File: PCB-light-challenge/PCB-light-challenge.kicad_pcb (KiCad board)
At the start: 4 copper layers, 79.9 x 79 mm, 27 parts, among them J1 Conn_01x16_Socket, J3 Conn_01x13_Socket, U2 AP9101CK, U3 SP8K32FRATB

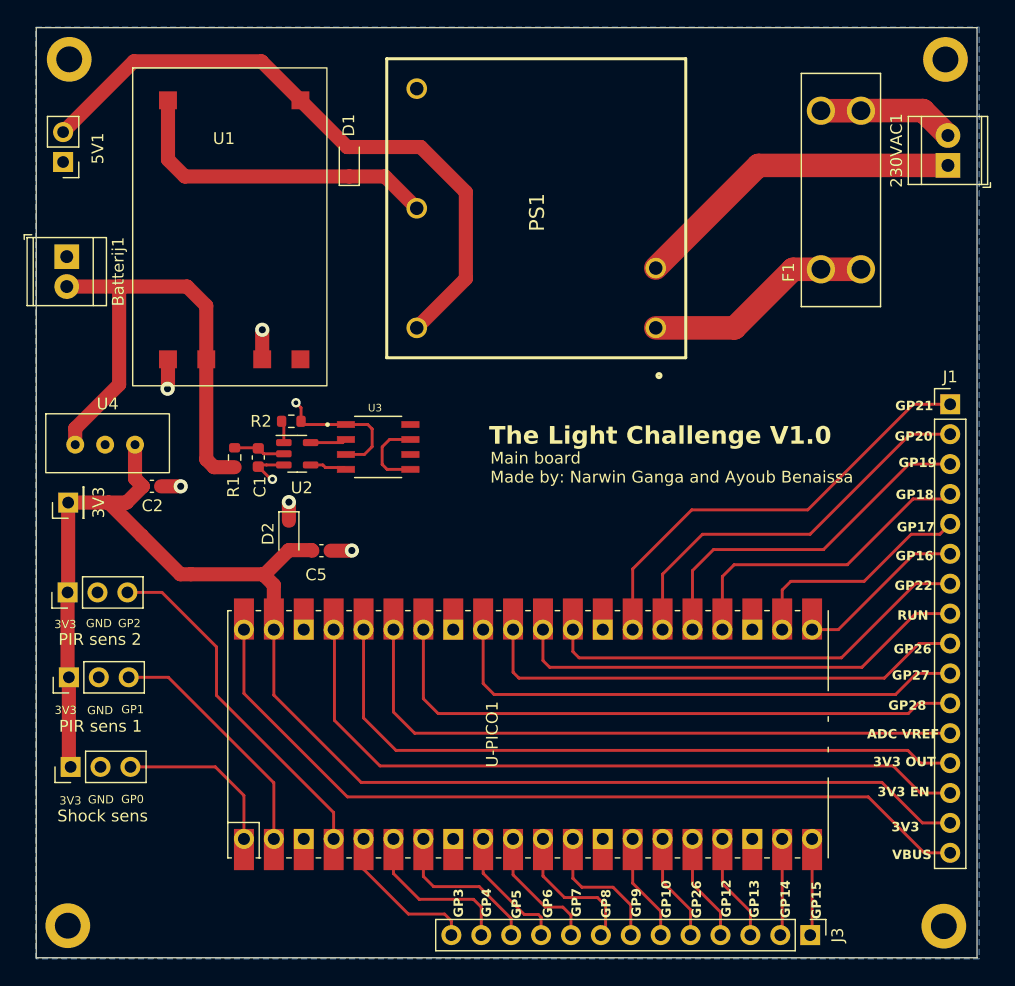
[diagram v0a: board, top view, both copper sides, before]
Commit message: Footprint van de eds protection device aangepast naar sod 523
https://nl.farnell.com/en-NL/rohm/rsb6-8smt2n/esd-protection-diode-sod-523-2/dp/2914120
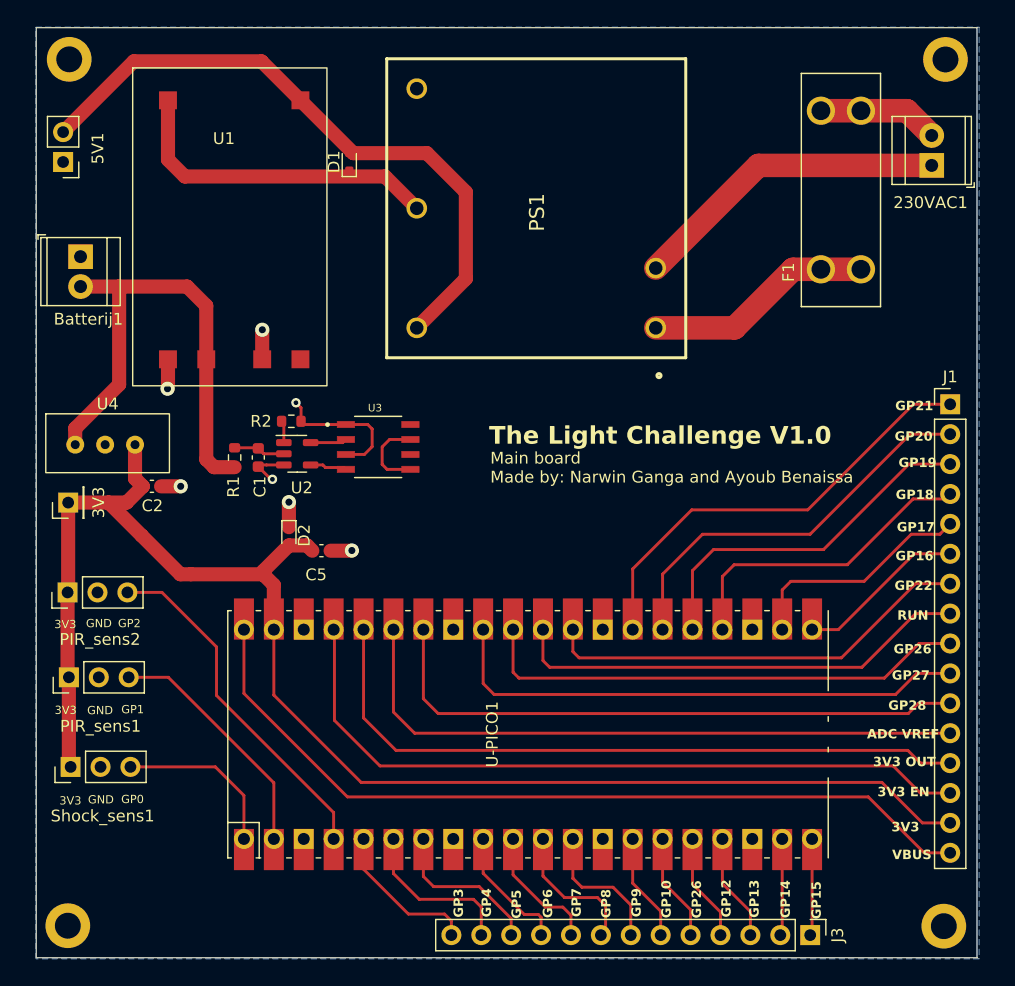
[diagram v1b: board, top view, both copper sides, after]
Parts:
- D1, D2: footprint Diode_SMD:D_SOD-323_HandSoldering -> Diode_SMD:D_SOD-523
- PIR_sens1: renamed from PIR sens 1
- PIR_sens2: renamed from PIR sens 2
- Shock_sens1: renamed from Shock sens
- moved 230VAC1 1.38 mm to (248.5, 84.8)
- moved Batterij1 1.17 mm to (176.2, 92.6)
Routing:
- net /Battery_charger/GNDAC: track 28.4 -> 27.1 mm
- net /Battery_charger/Fuse_in: track 11.7 -> 10.3 mm
- net BAT+: track 43.7 -> 42.5 mm
- net GND: track 26.0 -> 26.6 mm

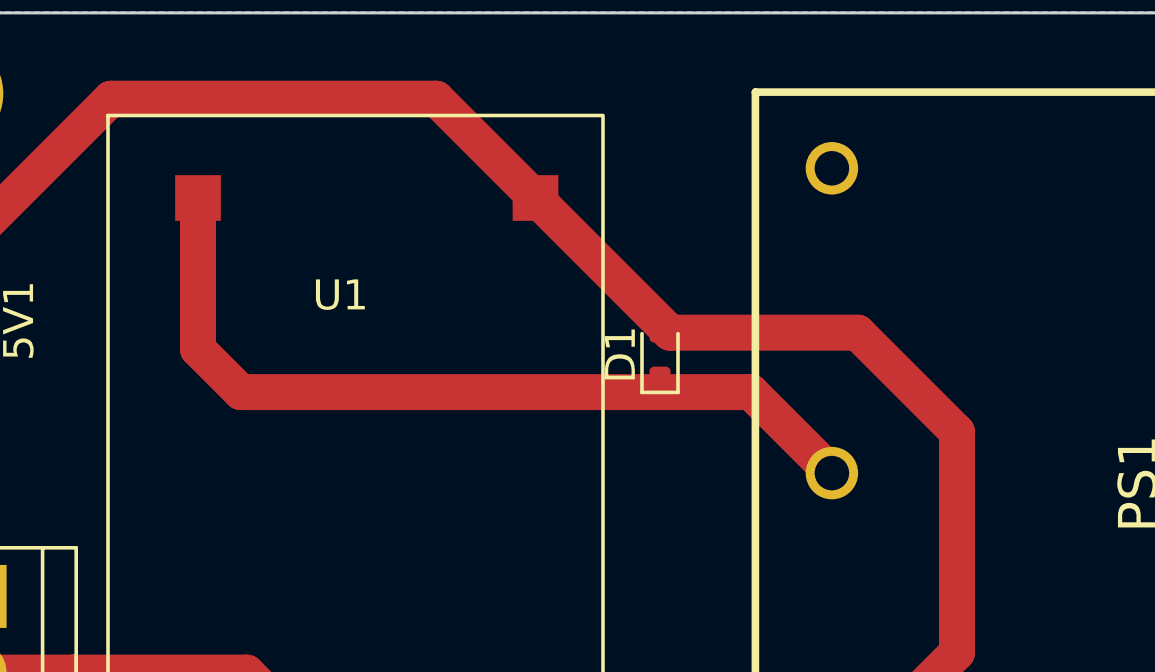
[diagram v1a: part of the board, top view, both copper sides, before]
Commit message: EDS device bij 230 verwijdert
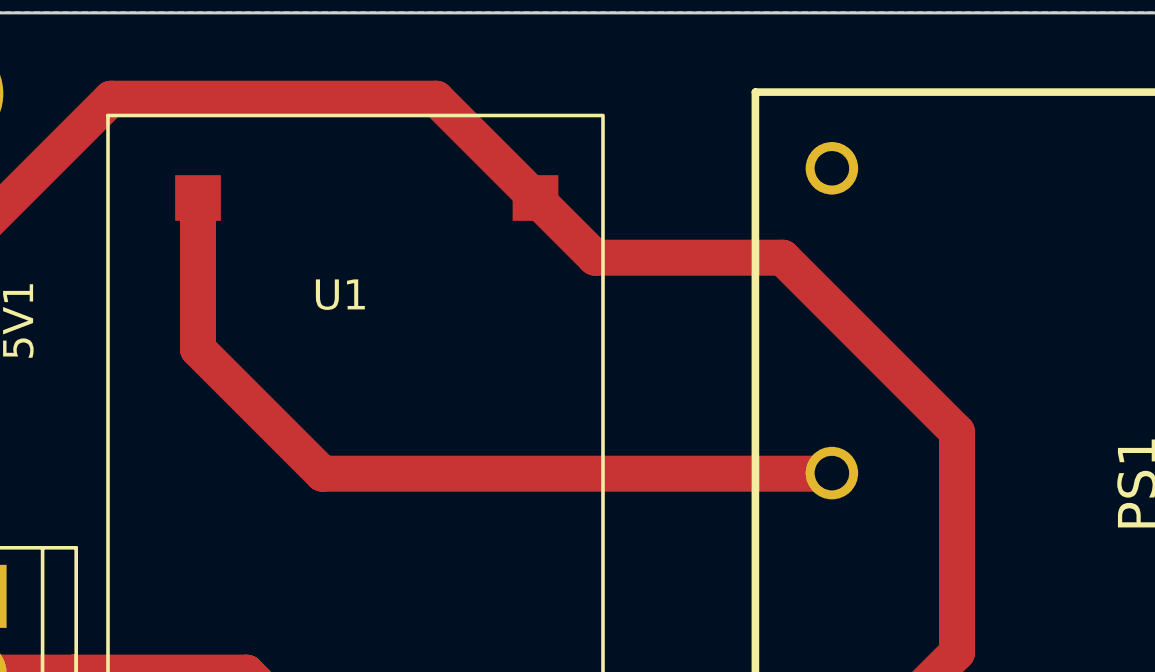
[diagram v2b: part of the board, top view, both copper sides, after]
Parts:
- removed D1: ESD9B3.3ST5G, Diode_SMD:D_SOD-523
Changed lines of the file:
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@@
   (net 40 "Net-(U3-Pad5)")
   (net 41 "GND")
-  (net 42 "Net-(D1-A1)")
+  (net 42 "Net-(PS1--VOUT)")
   (net 43 "/Battery_charger/Fuse_in")
   (net 44 "/Battery_charger/Fuse")
@@
       (scale (xyz 1 1 1))
       (rotate (xyz -90 0 0))
-    )
-  )
-  (footprint "Diode_SMD:D_SOD-523" (layer "F.Cu")
-    (at 199.03 84.53 90)
-    (descr "http://www.diodes.com/datasheets/ap02001.pdf p.144")
-    (tags "Diode SOD523")
-    (property "Sheetfile" "Battery_charger.kicad_sch")
-    (property "Sheetname" "Battery_charger")
-    (property "ki_description" "ESD protection diode, 3.3Vrwm, SOD-923")
-    (property "ki_keywords" "diode TVS ESD")
-    (attr smd)
-    (fp_text reference "D1" (at 0 -1.3 90) (layer "F.SilkS")
-        (effects (font (size 1 1) (thickness 0.15)))
-    )
-    (fp_text value "ESD9B3.3ST5G" (at 0 1.4 90) (layer "F.Fab")
-        (effects (font (size 1 1) (thickness 0.15)))
-    )
-    (fp_text user "${REFERENCE}" (at 0 -1.3 90) (layer "F.Fab")
-        (effects (font (size 1 1) (thickness 0.15)))
-    )
-    (fp_line (start -1.26 -0.6) (end -1.26 0.6)
-      (stroke (width 0.12) (type solid)) (layer "F.SilkS"))
-    (fp_line (start 0.7 -0.6) (end -1.26 -0.6)
-      (stroke (width 0.12) (type solid)) (layer "F.SilkS"))
-    (fp_line (start 0.7 0.6) (end -1.26 0.6)
-      (stroke (width 0.12) (type solid)) (layer "F.SilkS"))
-    (fp_line (start -1.25 -0.7) (end 1.25 -0.7)
-      (stroke (width 0.05) (type solid)) (layer "F.CrtYd"))
-    (fp_line (start -1.25 0.7) (end -1.25 -0.7)
-      (stroke (width 0.05) (type solid)) (layer "F.CrtYd"))
-    (fp_line (start 1.25 -0.7) (end 1.25 0.7)
-      (stroke (width 0.05) (type solid)) (layer "F.CrtYd"))
-    (fp_line (start 1.25 0.7) (end -1.25 0.7)
-      (stroke (width 0.05) (type solid)) (layer "F.CrtYd"))
-    (fp_line (start -0.65 -0.45) (end 0.65 -0.45)
-      (stroke (width 0.1) (type solid)) (layer "F.Fab"))
-    (fp_line (start -0.65 0.45) (end -0.65 -0.45)
-      (stroke (width 0.1) (type solid)) (layer "F.Fab"))
-    (fp_line (start -0.2 0) (end -0.35 0)
-      (stroke (width 0.1) (type solid)) (layer "F.Fab"))
-    (fp_line (start -0.2 0) (end 0.1 0.2)
-      (stroke (width 0.1) (type solid)) (layer "F.Fab"))
-    (fp_line (start -0.2 0.2) (end -0.2 -0.2)
-      (stroke (width 0.1) (type solid)) (layer "F.Fab"))
-    (fp_line (start 0.1 -0.2) (end -0.2 0)
-      (stroke (width 0.1) (type solid)) (layer "F.Fab"))
-    (fp_line (start 0.1 0) (end 0.25 0)
-      (stroke (width 0.1) (type solid)) (layer "F.Fab"))
-    (fp_line (start 0.1 0.2) (end 0.1 -0.2)
-      (stroke (width 0.1) (type solid)) (layer "F.Fab"))
-    (fp_line (start 0.65 -0.45) (end 0.65 0.45)
-      (stroke (width 0.1) (type solid)) (layer "F.Fab"))
-    (fp_line (start 0.65 0.45) (end -0.65 0.45)
-      (stroke (width 0.1) (type solid)) (layer "F.Fab"))
-    (pad "1" smd roundrect (at -0.7 0 270) (size 0.6 0.7) (layers "F.Cu" "F.Paste" "F.Mask") (roundrect_rratio 0.25)
-      (net 42 "Net-(D1-A1)") (pinfunction "A1") (pintype "passive"))
-    (pad "2" smd roundrect (at 0.7 0 270) (size 0.6 0.7) (layers "F.Cu" "F.Paste" "F.Mask") (roundrect_rratio 0.25)
-      (net 2 "+5V") (pinfunction "A2") (pintype "passive"))
-    (model "${KICAD6_3DMODEL_DIR}/Diode_SMD.3dshapes/D_SOD-523.wrl"
-      (offset (xyz 0 0 0))
-      (scale (xyz 1 1 1))
-      (rotate (xyz 0 0 0))
     )
   )
@@
       (net 45 "unconnected-(PS1-NC-Pad3)") (pinfunction "NC") (pintype "no_connect"))
     (pad "4" thru_hole circle (at 0 -10.15 90) (size 1.75 1.75) (drill 1.15) (layers "*.Cu" "*.Mask")
-      (net 42 "Net-(D1-A1)") (pinfunction "-VOUT") (pintype "passive"))
+      (net 42 "Net-(PS1--VOUT)") (pinfunction "-VOUT") (pintype "passive"))
     (pad "5" thru_hole circle (at -10.16 -10.15 90) (size 1.75 1.75) (drill 1.15) (layers "*.Cu" "*.Mask")
       (net 2 "+5V") (pinfunction "+VOUT") (pintype "passive"))
@@
       (net 41 "GND") (pinfunction "OUT-") (pintype "input"))
     (pad "5" smd rect (at 9.75 0) (size 1.524 1.524) (layers "F.Cu" "F.Paste" "F.Mask")
-      (net 42 "Net-(D1-A1)") (pinfunction "IN-") (pintype "bidirectional"))
+      (net 42 "Net-(PS1--VOUT)") (pinfunction "IN-") (pintype "bidirectional"))
     (pad "6" smd rect (at 21 0) (size 1.524 1.524) (layers "F.Cu" "F.Paste" "F.Mask")
       (net 2 "+5V") (pinfunction "IN+") (pintype "bidirectional"))
@@
   (segment (start 200.04 137.25) (end 192.62 129.83) (width 0.25) (layer "F.Cu") (net 1))
   (segment (start 180.73 76) (end 174.72 82.01) (width 1.2) (layer "F.Cu") (net 2))
+  (segment (start 204.76 98.63) (end 208.93 94.46) (width 1.2) (layer "F.Cu") (net 2))
+  (segment (start 191.57 76) (end 180.73 76) (width 1.2) (layer "F.Cu") (net 2))
+  (segment (start 208.93 87.11) (end 203.12 81.3) (width 1.2) (layer "F.Cu") (net 2))
+  (segment (start 208.93 94.46) (end 208.93 87.11) (width 1.2) (layer "F.Cu") (net 2))
+  (segment (start 196.87 81.3) (end 194.88 79.31) (width 1.2) (layer "F.Cu") (net 2))
+  (segment (start 203.12 81.3) (end 196.87 81.3) (width 1.2) (layer "F.Cu") (net 2))
+  (segment (start 194.88 79.31) (end 191.57 76) (width 1.2) (layer "F.Cu") (net 2))
   (segment (start 204.76 98.64) (end 204.76 98.63) (width 1.2) (layer "F.Cu") (net 2))
-  (segment (start 191.57 76) (end 180.73 76) (width 1.2) (layer "F.Cu") (net 2))
-  (segment (start 208.93 87.11) (end 205.62 83.8) (width 1.2) (layer "F.Cu") (net 2))
-  (segment (start 208.93 94.46) (end 208.93 87.11) (width 1.2) (layer "F.Cu") (net 2))
-  (segment (start 199.37 83.8) (end 194.88 79.31) (width 1.2) (layer "F.Cu") (net 2))
-  (segment (start 204.76 98.63) (end 208.93 94.46) (width 1.2) (layer "F.Cu") (net 2))
-  (segment (start 194.88 79.31) (end 191.57 76) (width 1.2) (layer "F.Cu") (net 2))
-  (segment (start 205.62 83.8) (end 199.37 83.8) (width 1.2) (layer "F.Cu") (net 2))
   (segment (start 175.75 107.18) (end 179.48 103.45) (width 1.2) (layer "F.Cu") (net 3))
   (segment (start 187.545 110.475) (end 189.29 110.475) (width 1.2) (layer "F.Cu") (net 3))
@@
   (via (at 184.71 112.1) (size 1.2) (drill 0.6) (layers "F.Cu" "B.Cu") (net 41))
   (via (at 183.59 103.81) (size 1.2) (drill 0.6) (layers "F.Cu" "B.Cu") (net 41))
-  (segment (start 185.06 85.78) (end 202.06 85.78) (width 1.2) (layer "F.Cu") (net 42))
-  (segment (start 202.06 85.78) (end 204.76 88.48) (width 1.2) (layer "F.Cu") (net 42))
+  (segment (start 204.74 88.5) (end 204.76 88.48) (width 1.2) (layer "F.Cu") (net 42))
+  (segment (start 187.78 88.5) (end 204.74 88.5) (width 1.2) (layer "F.Cu") (net 42))
+  (segment (start 183.63 84.35) (end 187.78 88.5) (width 1.2) (layer "F.Cu") (net 42))
   (segment (start 183.63 79.31) (end 183.63 84.35) (width 1.2) (layer "F.Cu") (net 42))
-  (segment (start 183.63 84.35) (end 185.06 85.78) (width 1.2) (layer "F.Cu") (net 42))
   (segment (start 246.395 80.195) (end 242.49 80.195) (width 2) (layer "F.Cu") (net 43))
   (segment (start 239.09 80.195) (end 242.49 80.195) (width 2) (layer "F.Cu") (net 43))
